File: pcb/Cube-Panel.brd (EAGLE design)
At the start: 100 x 100 mm, 348 parts, among them IC1 MBI5041-GP, IC2 ATTINY(261/461/861)V-MAZ, X2 JP8ER

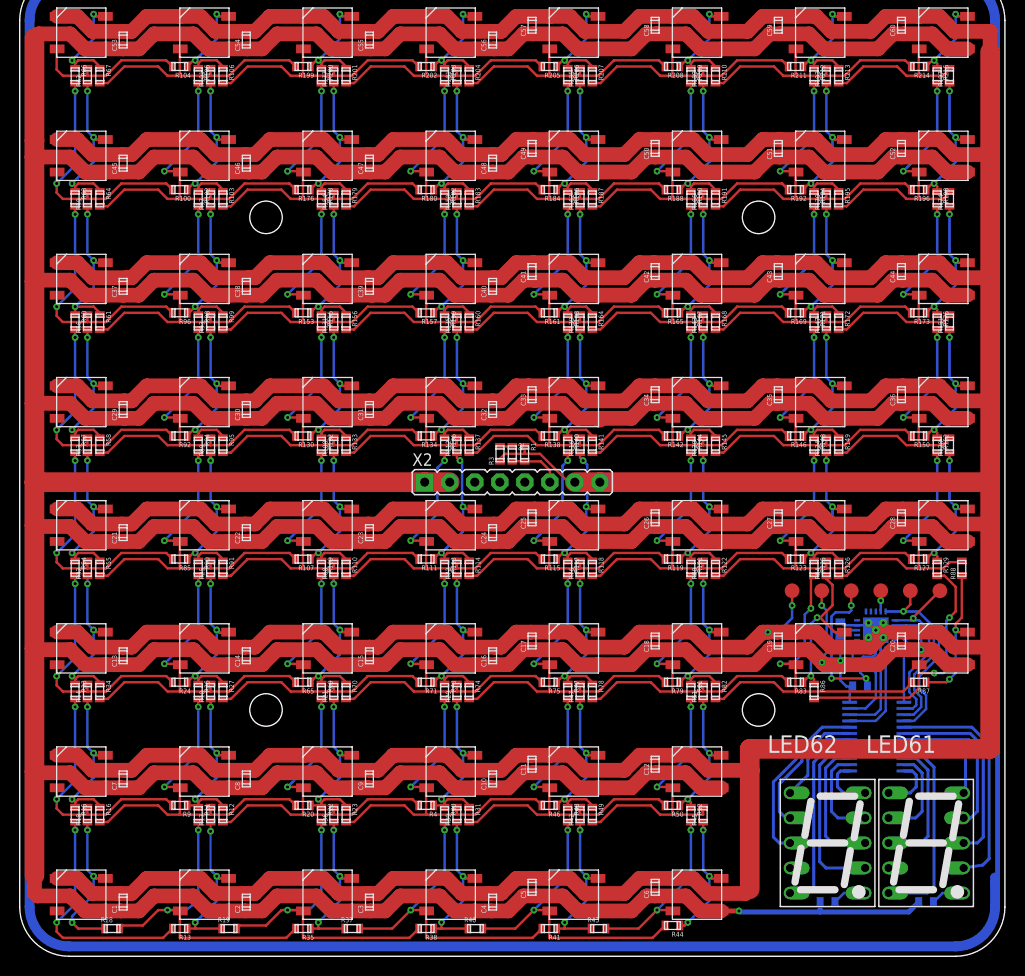
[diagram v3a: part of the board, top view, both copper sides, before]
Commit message: Added Select-Resistor for LED#1
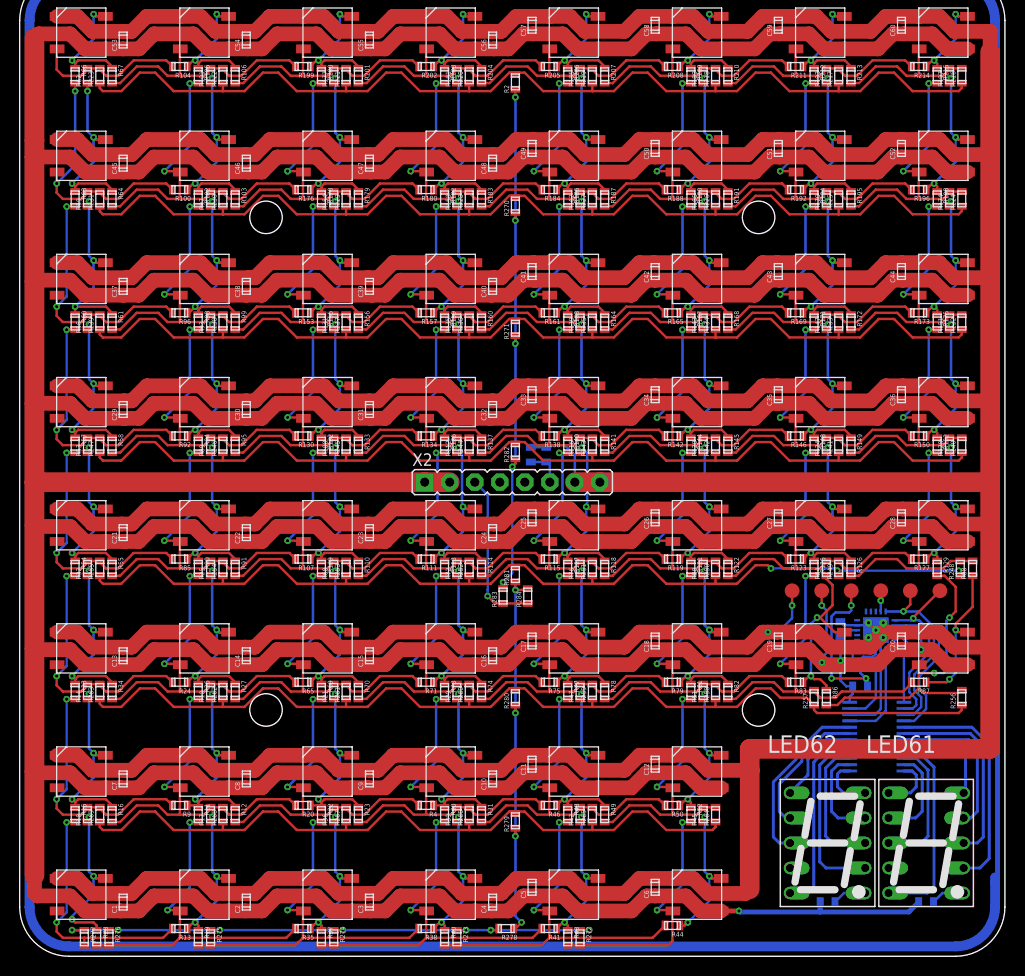
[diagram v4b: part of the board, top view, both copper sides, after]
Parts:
- added R216, R217, R218, R219, R220, R221, R222, R223, R224, R225, R226, R227, R228, R229, R230, R231, R232, R233, R234, R235, R236, R237, R238, R239, R240, R241, R242, R243, R244, R245, R246, R247, R248, R249, R250, R251, R252, R253, R254, R255, R256, R257, R258, R259, R260, R261, R262, R263, R264, R265, R266, R267, R268, R269, R270, R271, R272, R273, R274, R275, R276, R277, R278, R279, R280, R281, R282, R283, R284: (no value), _Passive:0603
- moved R2 37.8 mm to (0.31, 38.8), turned to 90 degrees
- moved R19 3.26 mm to (-31.9, -48.1), turned to 270 degrees
- moved R37 3.26 mm to (-19.4, -48.1), turned to 270 degrees
- moved R40 3.26 mm to (-6.88, -48.1), turned to 270 degrees
- moved R43 3.26 mm to (5.62, -48.1), turned to 270 degrees
- moved R3 3.13 mm to (1.88, 0.92), flipped to the bottom, turned to 270 degrees
- moved R1 2.19 mm to (3.44, 0.92), flipped to the bottom
- moved R28 1.82 mm to (-42.2, -48.1), turned to 270 degrees
- moved R86 1.40 mm to (31.9, -23.8)
- moved R103 1.25 mm to (-28.1, 26.9)
- moved R106 1.25 mm to (-28.1, 39.4)
- moved R110 1.25 mm to (-15.6, -10.6)
- moved R114 1.25 mm to (-3.12, -10.6)
- moved R118 1.25 mm to (9.38, -10.6)
- moved R12 1.25 mm to (-28.1, -35.6)
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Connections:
- new net LED-DATA: R283.P$1, R284.P$1, X2.3
- new net N$12: R2.P$2, R216.P$1, R217.P$1, R218.P$1, R219.P$1, R220.P$1, R221.P$1, R222.P$1, R223.P$1
- new net N$22: R224.P$1, R225.P$1, R226.P$1, R227.P$1, R228.P$1, R229.P$1, R230.P$1, R231.P$1, R270.P$2
- new net N$32: R232.P$1, R233.P$1, R234.P$1, R235.P$1, R236.P$1, R237.P$1, R238.P$1, R239.P$1, R271.P$2
- new net N$42: R240.P$1, R241.P$1, R242.P$1, R243.P$1, R244.P$1, R245.P$1, R246.P$1, R247.P$1, R282.P$2
- new net N$5: R2.P$1, R270.P$1, R271.P$1, R282.P$1, R283.P$2
- new net N$51: R248.P$1, R249.P$1, R250.P$1, R251.P$1, R252.P$1, R253.P$1, R254.P$1, R255.P$1, R281.P$2
- new net N$60: R256.P$1, R257.P$1, R258.P$1, R259.P$1, R260.P$1, R261.P$1, R262.P$1, R263.P$1, R280.P$2
- new net N$69: R264.P$1, R265.P$1, R266.P$1, R267.P$1, R268.P$1, R269.P$1, R279.P$2
- new net N$78: R272.P$1, R273.P$1, R274.P$1, R275.P$1, R276.P$1, R277.P$1, R278.P$2
- new net SLAVE_IN: X2.4
- new net SLAVE_OUT: X2.5
- net IN1: now also R277.P$2
- net IN10: now also R266.P$2
- net IN11: now also R265.P$2
- net IN12: now also R264.P$2
- net IN13: now also R263.P$2
- net IN14: now also R262.P$2
- net IN15: now also R261.P$2
- net IN16: now also R260.P$2
- net IN17: now also R259.P$2
- net IN18: now also R258.P$2
- net IN19: now also R257.P$2
- net IN2: now also R276.P$2
- net IN20: now also R256.P$2
- net IN21: now also R255.P$2
- net IN22: now also R254.P$2
- net IN23: now also R253.P$2
- net IN24: now also R252.P$2
- net IN25: now also R251.P$2
- net IN26: now also R250.P$2
- net IN27: now also R249.P$2
- net IN28: now also R248.P$2
- net IN29: now also R247.P$2
- net IN3: now also R275.P$2
- net IN30: now also R246.P$2
- net IN31: now also R245.P$2
- net IN32: now also R244.P$2
- net IN33: now also R243.P$2
- net IN34: now also R242.P$2
- net IN35: now also R241.P$2
- net IN36: now also R240.P$2
- net IN37: now also R239.P$2
- net IN38: now also R238.P$2
- net IN39: now also R237.P$2
- net IN4: now also R274.P$2
- net IN40: now also R236.P$2
- net IN41: now also R235.P$2
- net IN42: now also R234.P$2
- net IN43: now also R233.P$2
- net IN44: now also R232.P$2
- net IN45: now also R231.P$2
- net IN46: now also R230.P$2
- net IN47: now also R229.P$2
- net IN48: now also R228.P$2
- net IN49: now also R227.P$2
- net IN5: now also R273.P$2
- net IN50: now also R226.P$2
- net IN51: now also R225.P$2
- net IN52: now also R224.P$2
- net IN53: now also R223.P$2
- net IN54: now also R222.P$2
- net IN55: now also R221.P$2
- net IN56: now also R220.P$2
- net IN57: now also R219.P$2
- net IN58: now also R218.P$2
- net IN59: now also R217.P$2
- net IN6: now also R272.P$2
- net IN60: now also R216.P$2
- net IN7: now also R269.P$2
- net IN8: now also R268.P$2
- net IN9: now also R267.P$2
- net N$1: now also R278.P$1, R279.P$1, R280.P$1, R281.P$1, R284.P$2; no longer R2.P$1, R3.P$2
- net N$3: now also R3.P$2; no longer R2.P$2
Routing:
- net N$32: track 0.00 -> 104.7 mm
- net N$22: track 0.00 -> 104.7 mm
- net N$12: track 0.00 -> 104.7 mm
- net N$42: track 0.00 -> 104.5 mm
- net N$60: track 0.00 -> 102.9 mm
- net N$51: track 0.00 -> 102.1 mm, vias 0 -> 3
- net N$69: track 0.00 -> 74.8 mm
- net N$78: track 0.00 -> 59.4 mm, vias 0 -> 7
- net N$5: track 0.00 -> 53.8 mm, vias 0 -> 5
- net N$1: track 1.25 -> 38.8 mm, vias 0 -> 4
- net LED-DATA: track 0.00 -> 16.5 mm, vias 0 -> 1
- net IN6: track 18.0 -> 26.4 mm
- net IN5: track 33.0 -> 38.4 mm
- net IN4: track 32.9 -> 38.3 mm
- net IN3: track 34.1 -> 38.3 mm
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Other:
- board text added: "Every device is a smoke machine if you operate it wrong enough"
- board text removed: "ID"

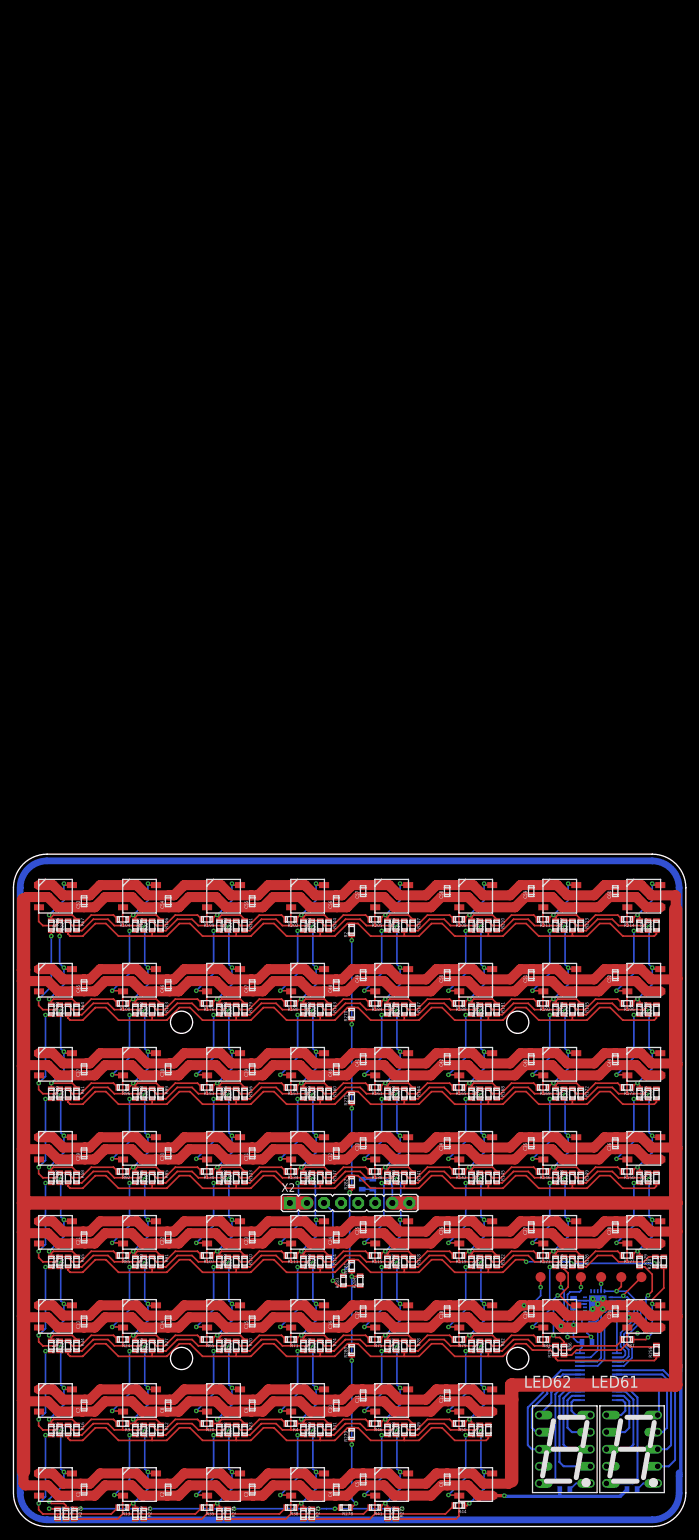
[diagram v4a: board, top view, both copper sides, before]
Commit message: Added Feedback-Trace for LED-Data. µC can now drive the LEDs. Added Single-Wire-UART-Bus for Communication.
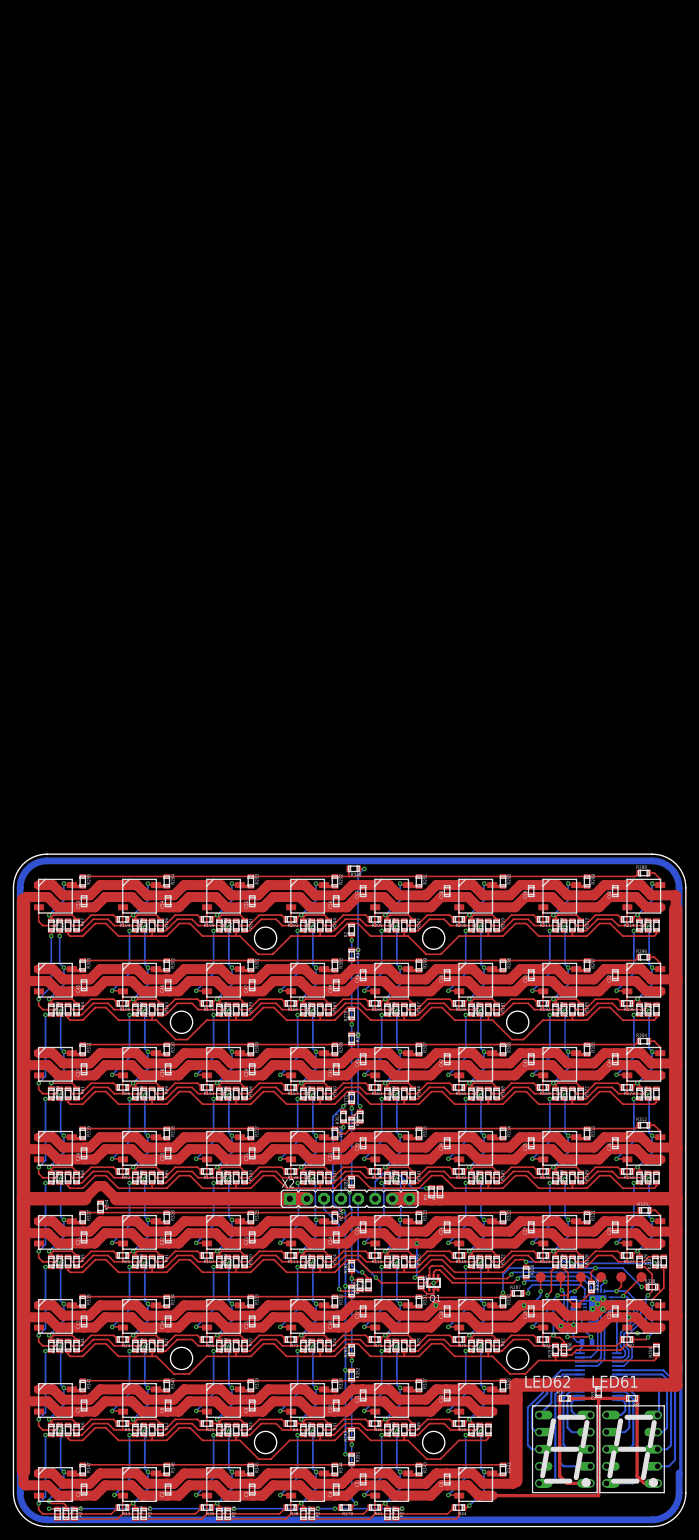
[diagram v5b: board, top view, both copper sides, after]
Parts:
- added C63, R285, R286, R287, R288, R289, R290, R291, R292, R293, R294, R295, R296, R297, R298, R299, R300, R301, R302, R303, R304, R305, R306, R307, R308, R309, R310, R311, R312, R313, R314, R315, R316, R317, R318, R319, R320, R321, R322, R323, R324, R325, R326, R327, R328, R329, R330, R331, R332, R333, R334, R335, R336, R337, R338, R339, R340, R341, R342, R343, R344, R345, R346, R347, R348, R349, R350, R351, R352, R353, R354, R355, R356, R357: (no value), _Passive:0603
- added Q1: DUAL_BJT_NPN_BIAS-PUMH2, _Transistor:SOT-363(SC-88)
- moved R7 13.6 mm to (32.0, -30.9), flipped to the top
- moved R8 13.6 mm to (42.0, -30.9), flipped to the top, turned to 180 degrees
- moved R3 10.4 mm to (12.2, -0.30), flipped to the top, turned to 90 degrees
- moved R1 10.1 mm to (13.4, -0.30), flipped to the top, turned to 90 degrees
- moved R283 3.80 mm to (2.81, -14.1)
- moved R284 0.62 mm to (1.56, -14.1)
- moved X2 0.62 mm to (0.00, -1.25)
- moved R44 0.31 mm to (16.2, -47.2)
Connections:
- removed net BUS-RX: IC2.17
- removed net BUS-TX: IC2.18
- removed net N$51: R248.P$1, R249.P$1, R250.P$1, R251.P$1, R252.P$1, R253.P$1, R254.P$1, R255.P$1, R281.P$2
- removed net SLAVE_IN: X2.4
- removed net SLAVE_OUT: X2.5
- new net LED-DATA-OUT: R356.P$1, R357.P$1, X2.4
- new net LED-DATA-OUT-UC: R287.P$1, R328.P$1, R329.P$1, R330.P$1, R331.P$1, R332.P$1, R333.P$1, R334.P$1, R335.P$1, R353.P$2
- new net LED-DATA-UC: R248.P$1, R249.P$1, R250.P$1, R251.P$1, R252.P$1, R253.P$1, R254.P$1, R255.P$1, R281.P$2, R286.P$1
- new net N$10: R312.P$1, R313.P$1, R314.P$1, R315.P$1, R316.P$1, R317.P$1, R318.P$1, R319.P$1, R355.P$2
- new net N$11: R320.P$1, R321.P$1, R322.P$1, R323.P$1, R324.P$1, R325.P$1, R326.P$1, R327.P$1, R354.P$2
- new net N$14: R336.P$1, R337.P$1, R338.P$1, R339.P$1, R340.P$1, R341.P$1, R352.P$2
- new net N$15: R342.P$1, R343.P$1, R344.P$1, R345.P$1, R346.P$1, R347.P$1, R351.P$2
- new net N$16: R351.P$1, R352.P$1, R353.P$1, R354.P$1, R357.P$2
- new net N$17: R348.P$1, R349.P$1, R350.P$1, R355.P$1, R356.P$2
- new net N$18: Q1.5, Q1.6, R285.P$2
- new net N$19: IC2.15, R287.P$2
- new net N$6: IC2.16, R286.P$2
- new net N$7: R288.P$1, R289.P$1, R290.P$1, R291.P$1, R292.P$1, R293.P$1, R294.P$1, R295.P$1, R348.P$2
- new net N$8: R296.P$1, R297.P$1, R298.P$1, R299.P$1, R300.P$1, R301.P$1, R302.P$1, R303.P$1, R349.P$2
- new net N$9: R304.P$1, R305.P$1, R306.P$1, R307.P$1, R308.P$1, R309.P$1, R310.P$1, R311.P$1, R350.P$2
- new net SERIAL-BUS: IC2.18, Q1.3, X2.5
- new net SERIAL-BUS-TX: IC2.17, Q1.2
- net GND: now also C63.P$2, Q1.1, Q1.4
- net OUT1: now also R347.P$2
- net OUT10: now also R338.P$2
- net OUT11: now also R337.P$2
- net OUT12: now also R336.P$2
- net OUT13: now also R335.P$2
- net OUT14: now also R334.P$2
- net OUT15: now also R333.P$2
- net OUT16: now also R332.P$2
- net OUT17: now also R331.P$2
- net OUT18: now also R330.P$2
- net OUT19: now also R329.P$2
- net OUT2: now also R346.P$2
- net OUT20: now also R328.P$2
- net OUT21: now also R327.P$2
- net OUT22: now also R326.P$2
- net OUT23: now also R325.P$2
- net OUT24: now also R324.P$2
- net OUT25: now also R323.P$2
- net OUT26: now also R322.P$2
- net OUT27: now also R321.P$2
- net OUT28: now also R320.P$2
- net OUT29: now also R319.P$2
- net OUT3: now also R345.P$2
- net OUT30: now also R318.P$2
- net OUT31: now also R317.P$2
- net OUT32: now also R316.P$2
- net OUT33: now also R315.P$2
- net OUT34: now also R314.P$2
- net OUT35: now also R313.P$2
- net OUT36: now also R312.P$2
- net OUT37: now also R311.P$2
- net OUT38: now also R310.P$2
- net OUT39: now also R309.P$2
- net OUT4: now also R344.P$2
- net OUT40: now also R308.P$2
- net OUT41: now also R307.P$2
- net OUT42: now also R306.P$2
- net OUT43: now also R305.P$2
- net OUT44: now also R304.P$2
- net OUT45: now also R303.P$2
- net OUT46: now also R302.P$2
- net OUT47: now also R301.P$2
- net OUT48: now also R300.P$2
- net OUT49: now also R299.P$2
- net OUT5: now also R343.P$2
- net OUT50: now also R298.P$2
- net OUT51: now also R297.P$2
- net OUT52: now also R296.P$2
- net OUT53: now also R295.P$2
- net OUT54: now also R294.P$2
- net OUT55: now also R293.P$2
- net OUT56: now also R292.P$2
- net OUT57: now also R291.P$2
- net OUT58: now also R290.P$2
- net OUT59: now also R289.P$2
- net OUT6: now also R342.P$2
- net OUT60: now also R288.P$2
- net OUT7: now also R341.P$2
- net OUT8: now also R340.P$2
- net OUT9: now also R339.P$2
- net VCC: now also C63.P$1, R285.P$1
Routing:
- net LED-DATA-UC: track 0.00 -> 102.9 mm, vias 0 -> 3
- net N$51: track 102.1 -> 0.00 mm, vias 3 -> 0
- net N$16: track 0.00 -> 93.6 mm, vias 0 -> 5
- net LED-DATA-OUT-UC: track 0.00 -> 92.9 mm, vias 0 -> 3
- net N$7: track 0.00 -> 84.0 mm
- net N$11: track 0.00 -> 83.7 mm
- net N$10: track 0.00 -> 83.6 mm
- net N$9: track 0.00 -> 83.0 mm
- net N$8: track 0.00 -> 83.0 mm
- net N$15: track 0.00 -> 62.6 mm
- net N$14: track 0.00 -> 62.6 mm
- net SERIAL-BUS: track 0.00 -> 51.3 mm, vias 0 -> 2
- net N$17: track 0.00 -> 41.3 mm, vias 0 -> 4
- net SERIAL-BUS-TX: track 0.00 -> 27.4 mm, vias 0 -> 1
- net VCC: track 965.6 -> 990.8 mm, vias 5 -> 6
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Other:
- board text added: "ID"
